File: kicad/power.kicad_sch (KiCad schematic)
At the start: 47 parts, among them J4 TYPE-C-31-M-12, Q7 BC847BW,115, U10 MC34063AD, U11 MC34063AD, U14 XC6206P332MR-G

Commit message: [kicad] Layout, mostly power traces + HS signal traces
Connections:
- net VBUCK10_IN: now reaches R60.2, U11.1 (SwC), U11.7 (Ipk), U11.8 (DC)
- net VBUCK5_IN: now reaches R59.2, U10.1 (SwC), U10.7 (Ipk), U10.8 (DC)
- net USB_DM renamed USB_DN
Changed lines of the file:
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@@
+    (effects (font (size 1.27 1.27)) (justify left bottom))
+  )
+  (label "VBUCK5_IN" (at 49.53 49.53 0) (fields_autoplaced)
+    (effects (font (size 1.27 1.27)) (justify left bottom))
+  )
+  (label "VBUCK10_IN" (at 52.07 105.41 0) (fields_autoplaced)
     (effects (font (size 1.27 1.27)) (justify left bottom))
   )
@@
     )
   )
-  (global_label "USB_DM" (shape input) (at 57.15 152.4 180) (fields_autoplaced)
+  (global_label "USB_DN" (shape input) (at 57.15 152.4 180) (fields_autoplaced)
     (effects (font (size 1.27 1.27)) (justify right))
-    (property "Intersheetrefs" "${INTERSHEET_REFS}" (at 46.6658 152.4 0)
+    (property "Intersheetrefs" "${INTERSHEET_REFS}" (at 46.7867 152.4 0)
       (effects (font (size 1.27 1.27)) (justify right) hide)
     )

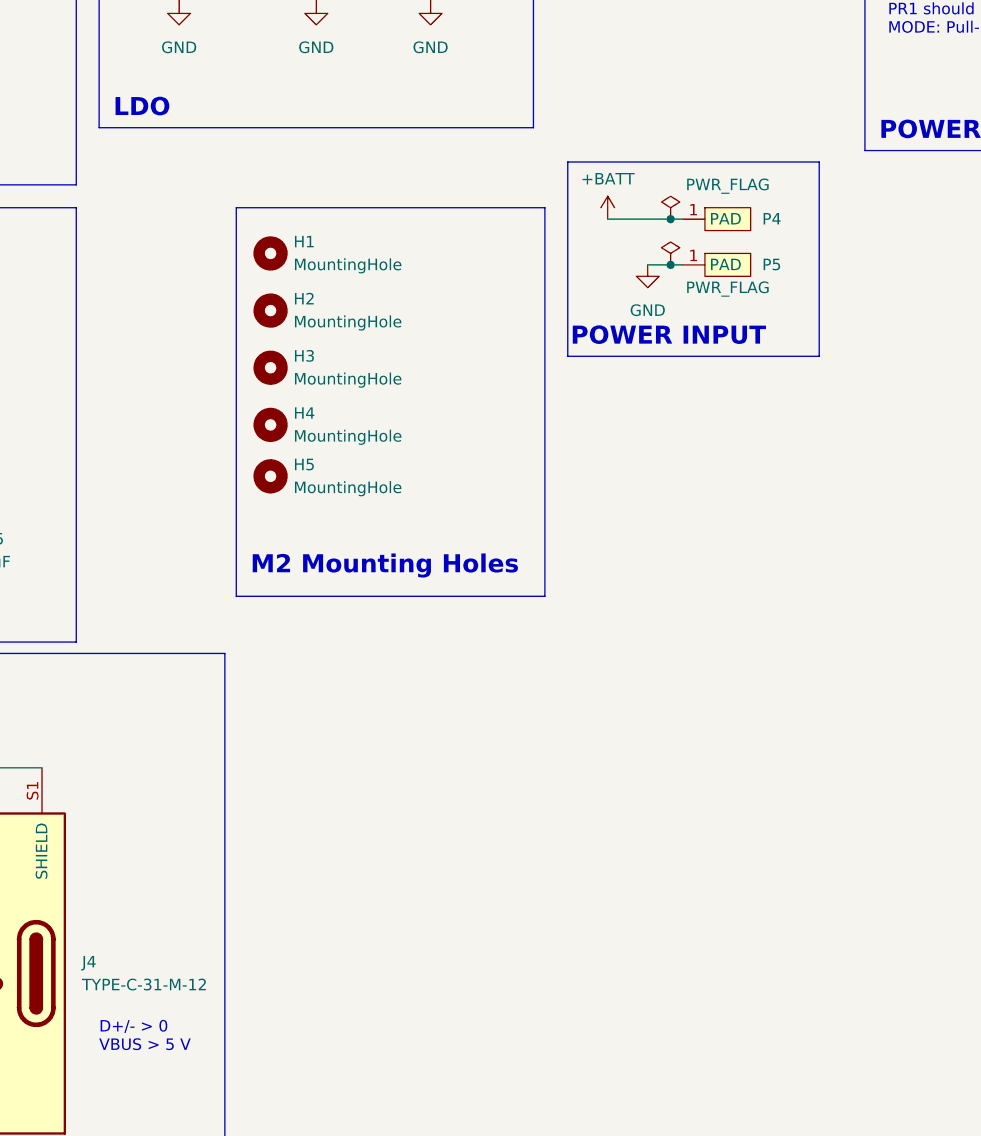
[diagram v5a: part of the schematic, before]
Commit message: [kicad] Routing ERC completed, Minor footprint issues
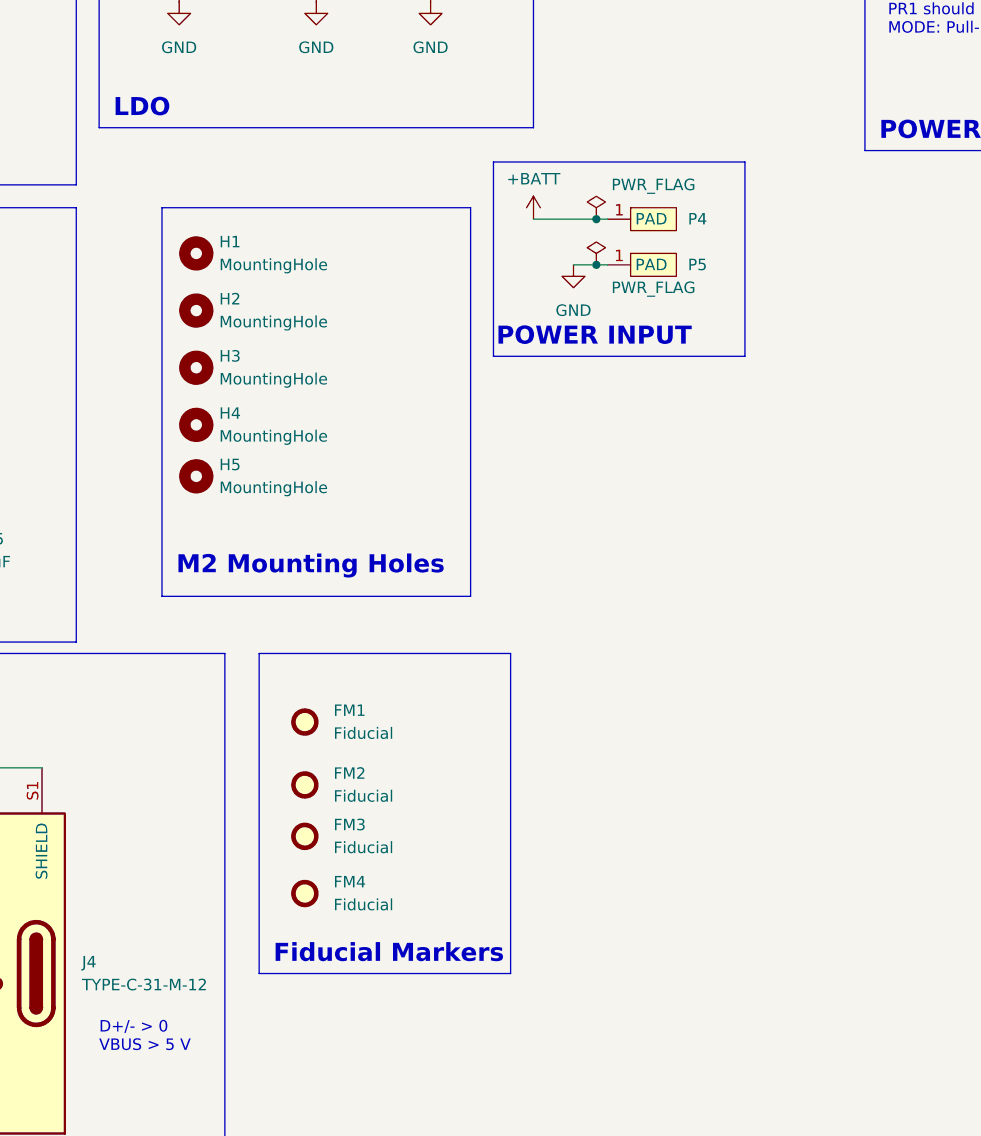
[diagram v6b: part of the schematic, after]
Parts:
- added FM1, FM2, FM3, FM4: Fiducial, Fiducial:Fiducial_1mm_Mask2mm, symbol Mechanical:Fiducial
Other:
- moved on the sheet: H1, H2, H3, H4, H5, P4, P5

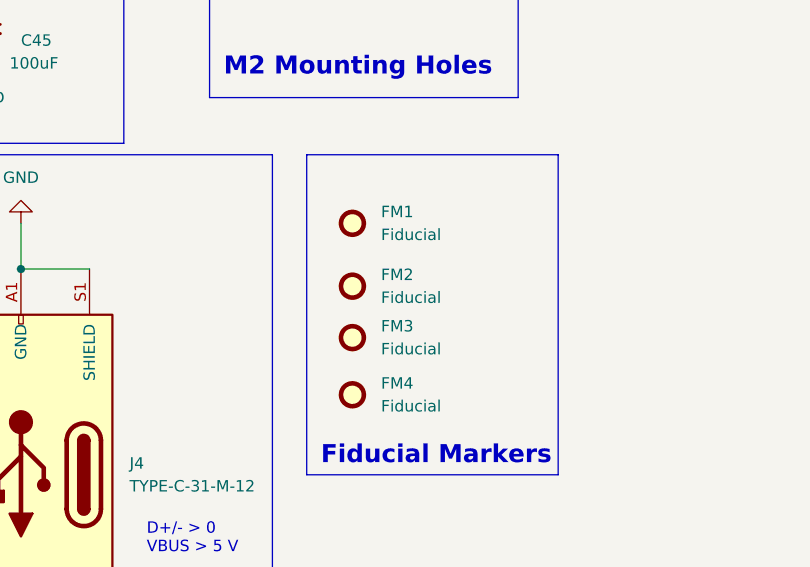
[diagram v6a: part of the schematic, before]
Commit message: [kicad] changed some footprints | TODO: Fix footprint of USB-ESD protection, recheck components, fix ERC errors
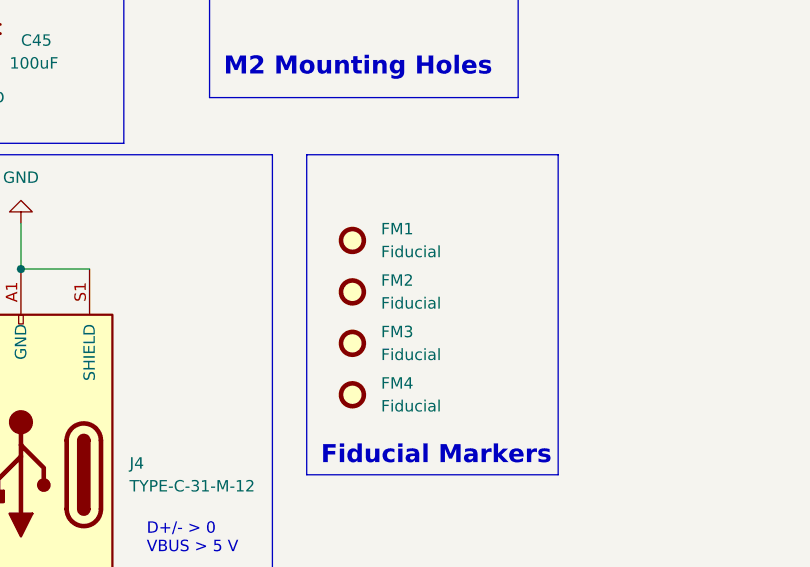
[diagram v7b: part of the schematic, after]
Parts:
- U10, U11: MFR.Part (none) -> MC34063; jlcpcb (none) -> C5349988
- U9: footprint bldc:TI_USB-ESD_TPD4S012 -> bldc:TI_R-PUSON-N6
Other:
- moved on the sheet: FM1, FM2, FM3
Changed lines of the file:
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@@
     )
   )
-  (symbol (lib_id "Mechanical:Fiducial") (at 132.08 121.92 0) (unit 1)
-    (in_bom yes) (on_board yes) (dnp no) (fields_autoplaced)
-    (property "Reference" "FM1" (at 135.255 120.65 0)
-      (effects (font (size 1.27 1.27)) (justify left))
-    )
-    (property "Value" "Fiducial" (at 135.255 123.19 0)
-      (effects (font (size 1.27 1.27)) (justify left))
-    )
-    (property "Footprint" "Fiducial:Fiducial_1mm_Mask2mm" (at 132.08 121.92 0)
-      (effects (font (size 1.27 1.27)) hide)
-    )
-    (property "Datasheet" "~" (at 132.08 121.92 0)
+  (symbol (lib_id "Mechanical:Fiducial") (at 132.08 123.825 0) (unit 1)
+    (in_bom yes) (on_board yes) (dnp no) (fields_autoplaced)
+    (property "Reference" "FM1" (at 135.255 122.555 0)
+      (effects (font (size 1.27 1.27)) (justify left))
+    )
+    (property "Value" "Fiducial" (at 135.255 125.095 0)
+      (effects (font (size 1.27 1.27)) (justify left))
+    )
+    (property "Footprint" "Fiducial:Fiducial_1mm_Mask2mm" (at 132.08 123.825 0)
+      (effects (font (size 1.27 1.27)) hide)
+    )
+    (property "Datasheet" "~" (at 132.08 123.825 0)
       (effects (font (size 1.27 1.27)) hide)
     )
@@
       (effects (font (size 1.27 1.27)))
     )
-    (property "Footprint" "bldc:TI_USB-ESD_TPD4S012" (at 39.37 158.75 0)
+    (property "Footprint" "bldc:TI_R-PUSON-N6" (at 39.37 158.75 0)
       (effects (font (size 1.27 1.27)) hide)
     )
@@
     )
     (property "Datasheet" "http://www.onsemi.com/pub_link/Collateral/MC34063A-D.PDF" (at 59.69 87.63 0)
+      (effects (font (size 1.27 1.27)) hide)
+    )
+    (property "jlcpcb" "C5349988" (at 72.39 90.17 0)
+      (effects (font (size 1.27 1.27)) hide)
+    )
+    (property "MFR.Part" "MC34063" (at 72.39 90.17 0)
       (effects (font (size 1.27 1.27)) hide)
     )
@@
     )
     (property "Datasheet" "http://www.onsemi.com/pub_link/Collateral/MC34063A-D.PDF" (at 57.15 36.83 0)
+      (effects (font (size 1.27 1.27)) hide)
+    )
+    (property "jlcpcb" "C5349988" (at 69.85 39.37 0)
+      (effects (font (size 1.27 1.27)) hide)
+    )
+    (property "MFR.Part" "MC34063" (at 69.85 39.37 0)
       (effects (font (size 1.27 1.27)) hide)
     )
@@
     )
   )
-  (symbol (lib_id "Mechanical:Fiducial") (at 132.08 134.62 0) (unit 1)
-    (in_bom yes) (on_board yes) (dnp no) (fields_autoplaced)
-    (property "Reference" "FM3" (at 135.255 133.35 0)
-      (effects (font (size 1.27 1.27)) (justify left))
-    )
-    (property "Value" "Fiducial" (at 135.255 135.89 0)
-      (effects (font (size 1.27 1.27)) (justify left))
-    )
-    (property "Footprint" "Fiducial:Fiducial_1mm_Mask2mm" (at 132.08 134.62 0)
-      (effects (font (size 1.27 1.27)) hide)
-    )
-    (property "Datasheet" "~" (at 132.08 134.62 0)
+  (symbol (lib_id "Mechanical:Fiducial") (at 132.08 135.255 0) (unit 1)
+    (in_bom yes) (on_board yes) (dnp no) (fields_autoplaced)
+    (property "Reference" "FM3" (at 135.255 133.985 0)
+      (effects (font (size 1.27 1.27)) (justify left))
+    )
+    (property "Value" "Fiducial" (at 135.255 136.525 0)
+      (effects (font (size 1.27 1.27)) (justify left))
+    )
+    (property "Footprint" "Fiducial:Fiducial_1mm_Mask2mm" (at 132.08 135.255 0)
+      (effects (font (size 1.27 1.27)) hide)
+    )
+    (property "Datasheet" "~" (at 132.08 135.255 0)
       (effects (font (size 1.27 1.27)) hide)
     )
@@
     )
   )
-  (symbol (lib_id "Mechanical:Fiducial") (at 132.08 128.905 0) (unit 1)
-    (in_bom yes) (on_board yes) (dnp no) (fields_autoplaced)
-    (property "Reference" "FM2" (at 135.255 127.635 0)
-      (effects (font (size 1.27 1.27)) (justify left))
-    )
-    (property "Value" "Fiducial" (at 135.255 130.175 0)
-      (effects (font (size 1.27 1.27)) (justify left))
-    )
-    (property "Footprint" "Fiducial:Fiducial_1mm_Mask2mm" (at 132.08 128.905 0)
-      (effects (font (size 1.27 1.27)) hide)
-    )
-    (property "Datasheet" "~" (at 132.08 128.905 0)
-      (effects (font (size 1.27 1.27)) hide)
-    )
+  (symbol (lib_id "Mechanical:Fiducial") (at 132.08 129.54 0) (unit 1)
+    (in_bom yes) (on_board yes) (dnp no) (fields_autoplaced)
+    (property "Reference" "FM2" (at 135.255 128.27 0)
+      (effects (font (size 1.27 1.27)) (justify left))
+    )
+    (property "Value" "Fiducial" (at 135.255 130.81 0)
+      (effects (font (size 1.27 1.27)) (justify left))
+    )
+    (property "Footprint" "Fiducial:Fiducial_1mm_Mask2mm" (at 132.08 129.54 0)
+      (effects (font (size 1.27 1.27)) hide)
+    )
+    (property "Datasheet" "~" (at 132.08 129.54 0)
+      (effects (font (size 1.27 1.27)) hide)
+    )
